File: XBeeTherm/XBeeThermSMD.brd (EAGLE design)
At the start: 31.8 x 20.3 mm, 20 parts, among them IC1 TLC272D

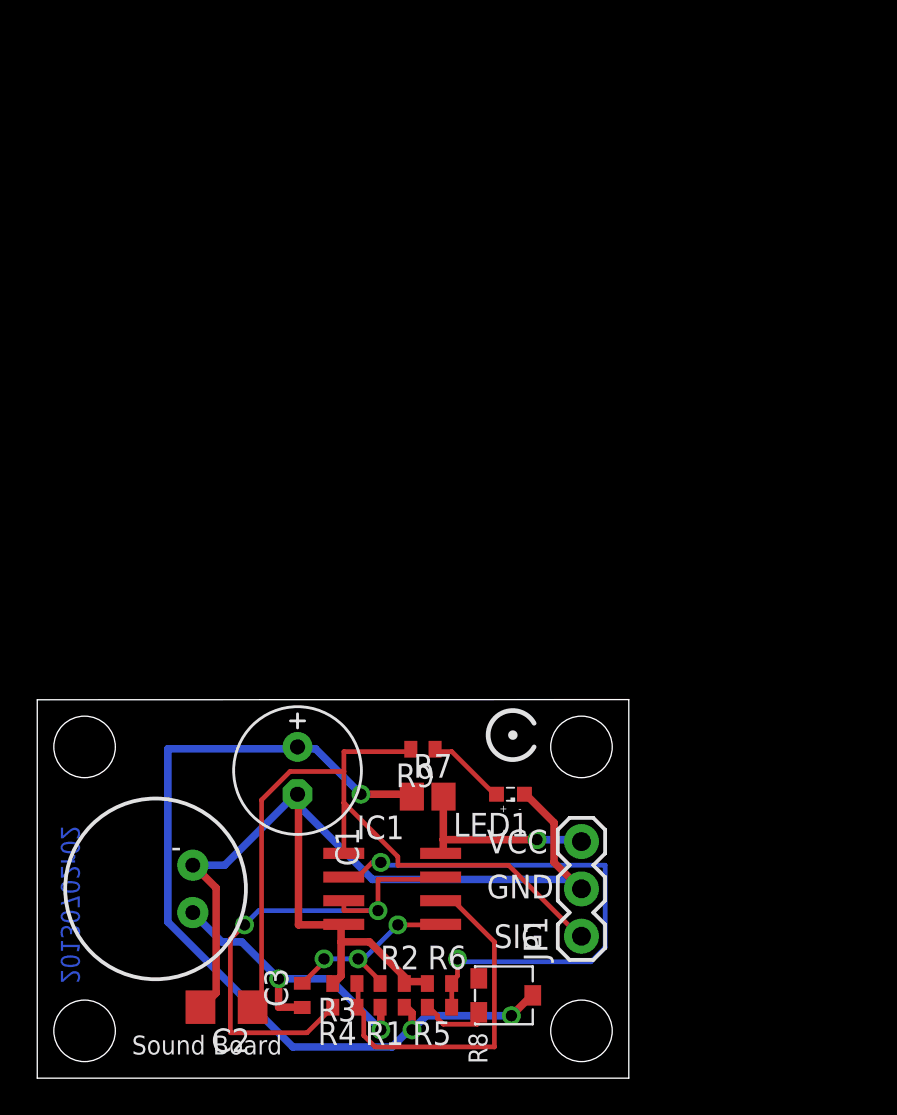
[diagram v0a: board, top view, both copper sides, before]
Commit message: Early revision (not yet final) of XBee therm board
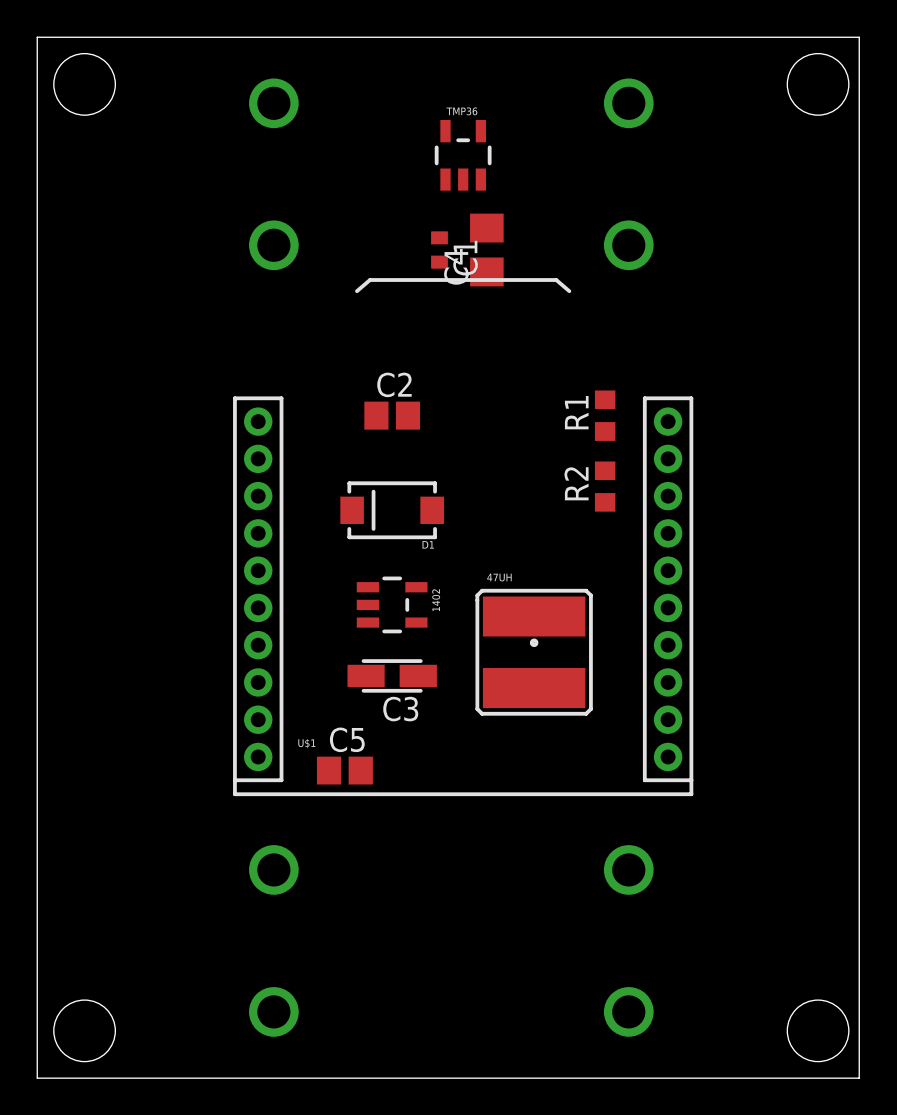
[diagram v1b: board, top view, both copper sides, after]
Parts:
- removed IC1: TLC272D, linear:SO08
- removed JP1: (no value), SparkFun-Connectors:1X03
- removed LED1: (no value), led:SML0603
- removed R3, R6, R9: 1k, resistor:R0402
- removed R4: 100k, resistor:R0402
- removed R5: 30k, resistor:R0402
- removed R7: 12R, resistor:R0805
- removed R8: TRIMPOT 25K, SparkFun-Electromechanical:TRIMPOT_TC33
- added 1402: NCP1402, SparkFun-PowerIC:SOT23-5
- added 47UH: (no value), SparkFun-Passives:CR54
- added C4: 2.2uF, resistor:R/2012-12R
- added C5: 1uF, resistor:C0805
- added D1: MBRA140, SparkFun-DiscreteSemi:SMA-DIODE
- added TMP36: TMP36, Sensors:SOT23-5
- added U$2, U$3: BATTERY-AA, Connectors_and_Brackets:BATTERY_AA_CLIPS
- C1: value 470uF -> 0.1uF; device resistor:E2,5-7 -> resistor:C0402
- C2: value 22uF -> 10uF; device resistor:C1206 -> resistor:C0805
- C3: value 0.1uF -> 68uF; device resistor:C1005 -> resistor:CT3216
- R1: value 22k -> 200k; device resistor:R0402 -> resistor:R0603
- R2: device resistor:R0402 -> resistor:R0603
- U$1: value MIC9.7MM -> XBEE-1B2; device SparkFun-Sensors:MIC-9.7MM -> SparkFun-RF:XBEE-SILK
- moved STANDOFF4 57.4 mm to (2.54, 53.3)
- moved STANDOFF1 53.1 mm to (41.9, 53.3)
- moved STANDOFF3 39.4 mm to (41.9, 2.54)
- moved R1 33.7 mm to (30.5, 35.6), turned to 90 degrees
- moved C2 33.0 mm to (19.1, 35.6), turned to 0 degrees
- moved STANDOFF2 30.7 mm to (2.54, 2.54)
- moved R2 29.0 mm to (30.5, 31.8), turned to 90 degrees
- moved C1 29.0 mm to (21.6, 44.5)
- moved C3 17.8 mm to (19.1, 21.6), turned to 180 degrees
- moved U$1 17.3 mm to (22.9, 15.2), turned to 0 degrees
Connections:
- removed net N$5: C3.2, IC1.5, R2.1
- removed net N$6: R5.2, R8.3
- removed net N$7: C3.1, R1.2, U$1.1
- removed net N$8: LED1.A, R9.1
- removed net SIG: C2.1, IC1.1, JP1.1, R9.2
- removed net VCC: IC1.8, JP1.3, R7.2
- new net 3.3V: 1402.1, 1402.2, C1.1, C3.+, C4.+, C5.1, D1.C, TMP36.2, TMP36.4, U$1.1
- new net BAT+: 47UH.P$1, C2.1, U$3.PWR@1, U$3.PWR@2
- net GND: now also 1402.4, C1.2, C3.-, C4.-, C5.2, R2.1, TMP36.5, U$1.10, U$2.GND@1, U$2.GND@2; no longer C1.-, IC1.4, JP1.2, LED1.C, R2.2, R3.2, R6.1, U$1.2
- net N$1: now also 1402.5, 47UH.P$2, D1.A; no longer C1.+, R1.1, R7.1, R8.2
- net N$2: now also U$2.PWR@1, U$2.PWR@2, U$3.GND@1, U$3.GND@2; no longer IC1.2, R5.1, R6.2
- net N$3: now also R1.1, R2.2, U$1.20; no longer IC1.3, IC1.7, R4.2
- net N$4: now also R1.2, TMP36.1; no longer IC1.6, R3.1, R4.1
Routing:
- net GND: track 58.9 -> 0.00 mm
- net N$1: track 48.5 -> 0.00 mm, vias 3 -> 0
- net SIG: track 41.5 -> 0.00 mm
- net N$2: track 29.9 -> 0.00 mm, vias 2 -> 0
- net N$3: track 27.2 -> 0.00 mm, vias 2 -> 0
- net N$4: track 19.7 -> 0.00 mm
- net N$7: track 16.8 -> 0.00 mm, vias 2 -> 0
- net N$5: track 10.6 -> 0.00 mm, vias 3 -> 0
- net VCC: track 10.6 -> 0.00 mm, vias 1 -> 0
- net N$8: track 4.30 -> 0.00 mm
- net N$6: track 3.84 -> 0.00 mm
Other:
- board size 31.8 x 20.3 mm -> 44.1 x 55.9 mm
- board text removed: "+"
- board text removed: "-"
- board text removed: "0.1uF"
- board text removed: "100k"
- board text removed: "12R"
- board text removed: "1k"
- board text removed: "20130702r02"
- board text removed: "22k"
- board text removed: "22uF"
- board text removed: "30.1k"
- board text removed: "30k trim"
- board text removed: "470uF"
- board text removed: "GND"
- board text removed: "LED"
- board text removed: "SIG"
- board text removed: "Sound Board"
- board text removed: "TLC272"
- board text removed: "VCC"

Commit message: First fab of the XBee therm board
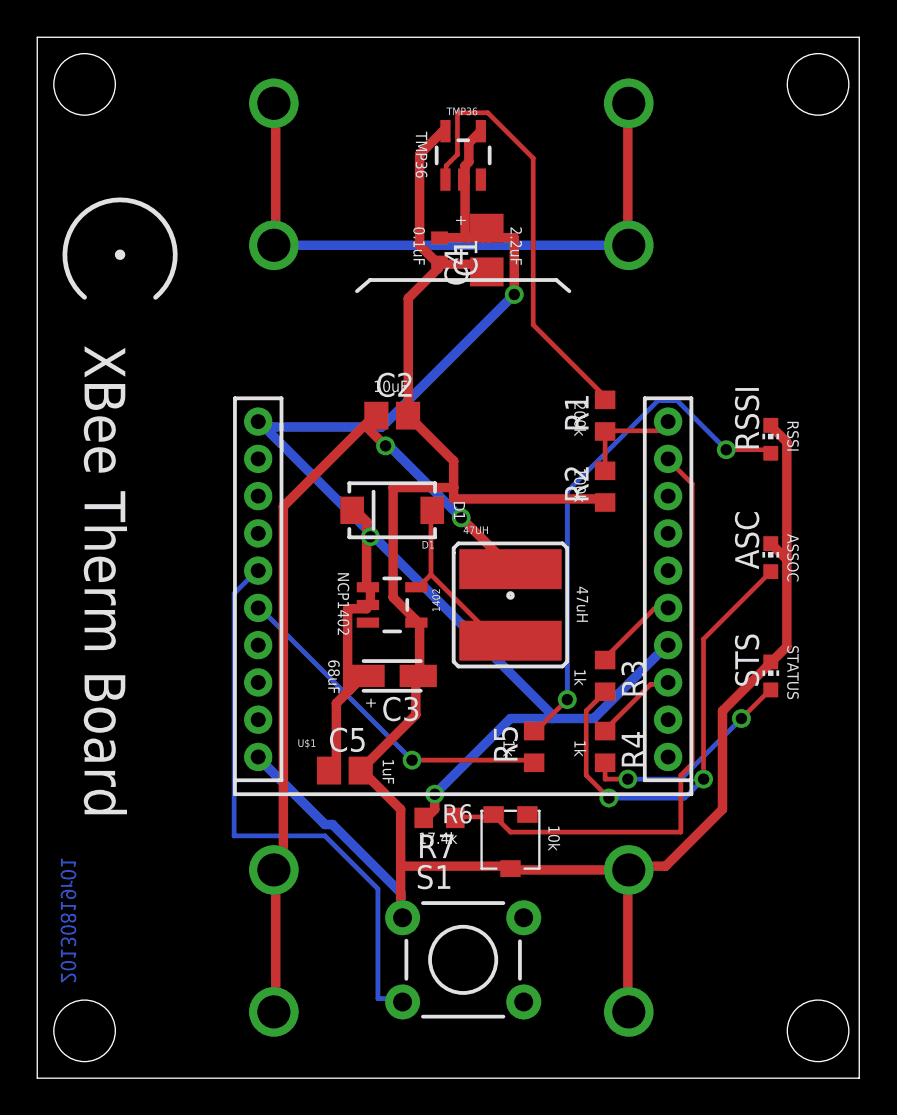
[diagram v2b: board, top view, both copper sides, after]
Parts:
- added ASC, RSSI, STS: (no value), led:CHIP-LED0603
- added R3, R4, R5: 1k, resistor:R0603
- added R6: 10K, SparkFun-Electromechanical:TRIMPOT_TC33
- added R7: 17.5k, resistor:R0603
- added S1: SWITCH-MOMENTARY-2PTH, SparkFun-Electromechanical:TACTILE-PTH
- moved 47UH 2.84 mm to (25.4, 25.4)
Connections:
- new net N$10: S1.3, U$1.5
- new net N$13: R5.2, RSSI.A
- new net N$5: R3.1, U$1.15
- new net N$6: R4.1, U$1.13
- new net N$7: ASC.A, R3.2
- new net N$8: R4.2, STS.A
- new net N$9: R6.3, R7.1, U$1.19
- new net RSSI: R5.1, U$1.6
- net 3.3V: now also R7.2, U$1.14
- net GND: now also ASC.C, R6.2, RSSI.C, S1.1, STS.C
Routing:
- net GND: track 0.00 -> 125.3 mm
- net 3.3V: track 0.00 -> 88.5 mm, vias 0 -> 3
- net BAT+: track 0.00 -> 46.2 mm, vias 0 -> 2
- net N$2: track 0.00 -> 34.5 mm
- net N$9: track 0.00 -> 33.4 mm
- net N$10: track 0.00 -> 31.0 mm
- net N$13: track 0.00 -> 27.8 mm, vias 0 -> 2
- net N$7: track 0.00 -> 24.8 mm, vias 0 -> 2
- net N$4: track 0.00 -> 23.5 mm
- net RSSI: track 0.00 -> 18.3 mm, vias 0 -> 1
- net N$8: track 0.00 -> 11.7 mm, vias 0 -> 2
- net N$1: track 0.00 -> 10.4 mm
- net N$3: track 0.00 -> 5.96 mm
- net N$5: track 0.00 -> 4.60 mm
- net N$6: track 0.00 -> 4.49 mm
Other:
- board text added: "+"
- board text added: "0.1uF"
- board text added: "100k"
- board text added: "10k"
- board text added: "10uF"
- board text added: "17.4k"
- board text added: "1k"
- board text added: "1uF"
- board text added: "2.2uF"
- board text added: "200k"
- board text added: "20130819r01"
- board text added: "47uH"
- board text added: "68uF"
- board text added: "ASSOC"
- board text added: "D1"
- board text added: "NCP1402"
- board text added: "RSSI"
- board text added: "STATUS"
- board text added: "TMP36"
- board text added: "XBee Therm Board"

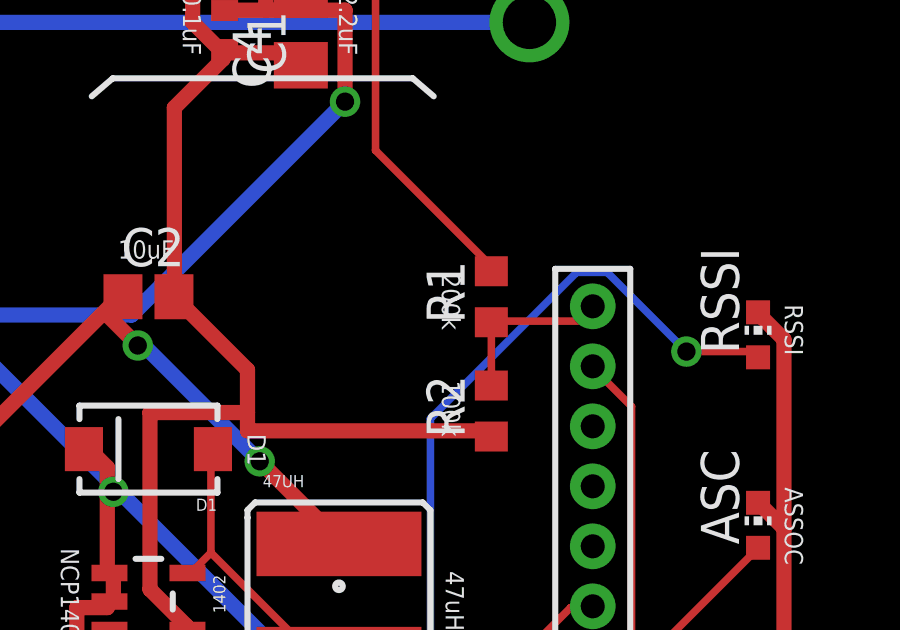
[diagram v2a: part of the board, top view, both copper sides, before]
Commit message: Update for the 0 ohm jumper change to the board
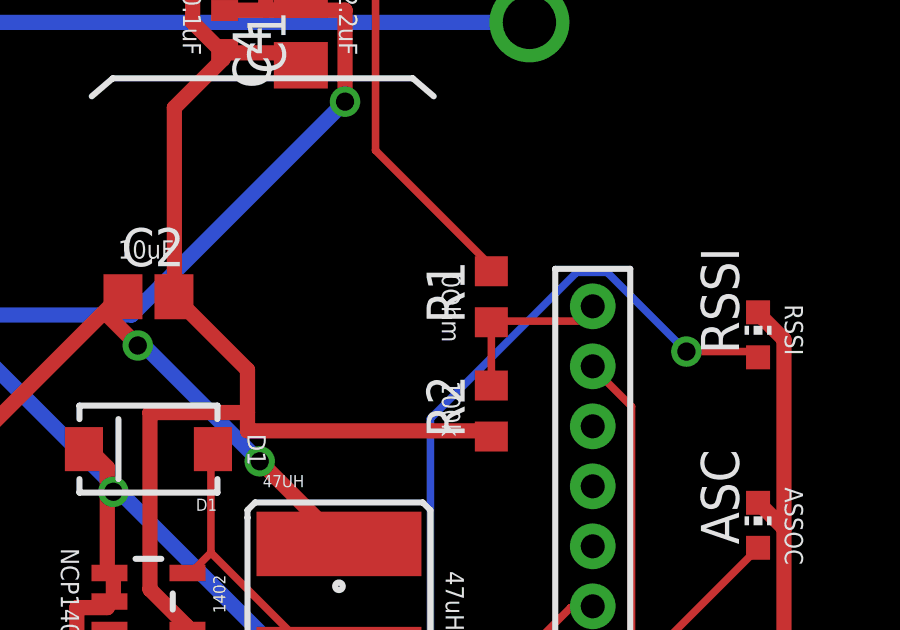
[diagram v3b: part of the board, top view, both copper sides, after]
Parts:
- R1: value 200k -> 0 (Bridge)
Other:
- board text added: "0Ohm"
- board text removed: "200k"
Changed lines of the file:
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@@
 <text x="2.54" y="39.37" size="2.1844" layer="21" font="vector" ratio="15" rot="SR270">XBee Therm Board</text>
 <text x="18.034" y="36.83" size="0.6096" layer="21" font="vector" ratio="15">10uF</text>
-<text x="28.829" y="36.322" size="0.6096" layer="21" font="vector" ratio="15" rot="SR270">200k</text>
+<text x="28.829" y="36.322" size="0.6096" layer="21" font="vector" ratio="15" rot="SR270">0Ohm</text>
 <text x="28.829" y="32.766" size="0.6096" layer="21" font="vector" ratio="15" rot="SR270">100k</text>
 <text x="28.956" y="26.416" size="0.6096" layer="21" font="vector" ratio="15" rot="SR270">47uH</text>
@@
 <element name="C1" library="resistor" package="C0402" value="0.1uF" x="21.59" y="44.45" rot="R270"/>
 <element name="C4" library="resistor" package="R/2012-12R" value="2.2uF" x="24.13" y="44.45" rot="R90"/>
-<element name="R1" library="resistor" package="R0603" value="200k" x="30.48" y="35.56" rot="R90"/>
+<element name="R1" library="resistor" package="R0603" value="0 (Bridge)" x="30.48" y="35.56" rot="R90"/>
 <element name="R2" library="resistor" package="R0603" value="100k" x="30.48" y="31.75" rot="R90"/>
 <element name="C5" library="resistor" package="C0805" value="1uF" x="16.51" y="16.51"/>

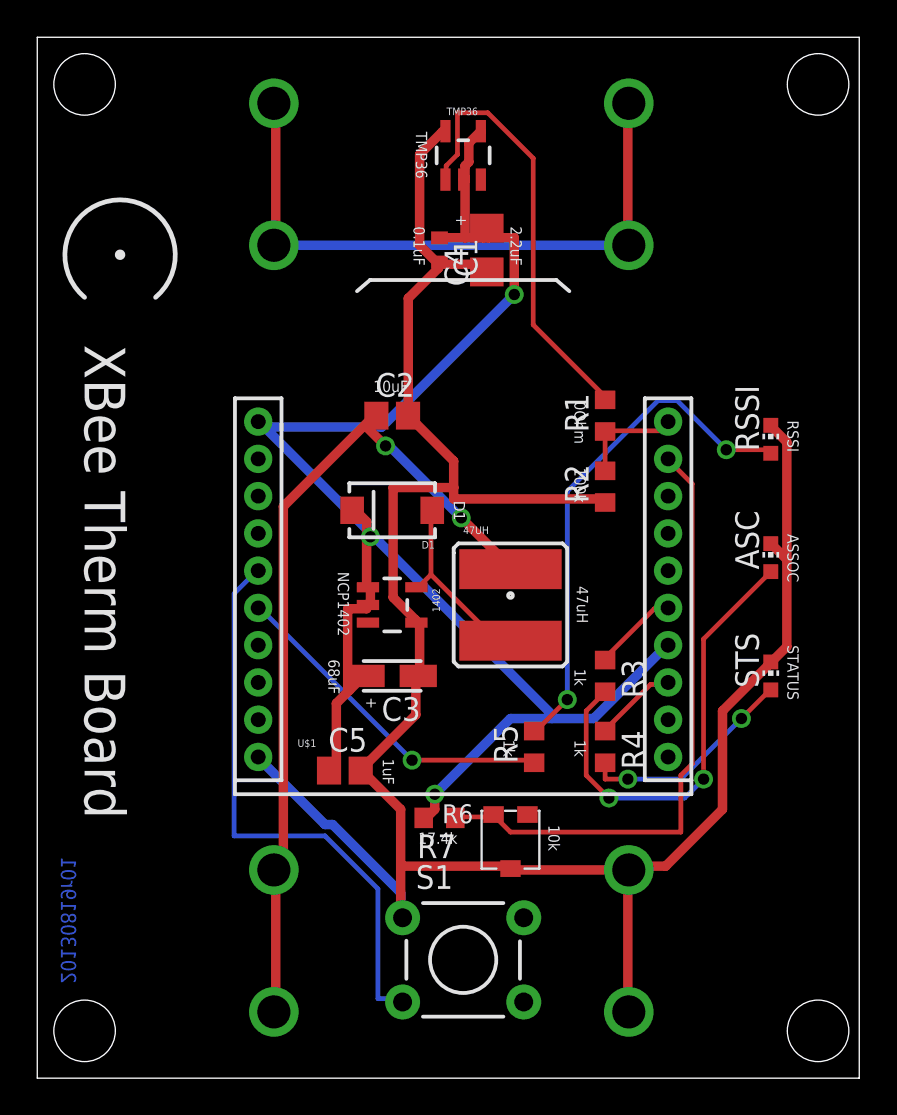
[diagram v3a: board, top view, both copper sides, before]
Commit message: Adding battery undervoltage protection
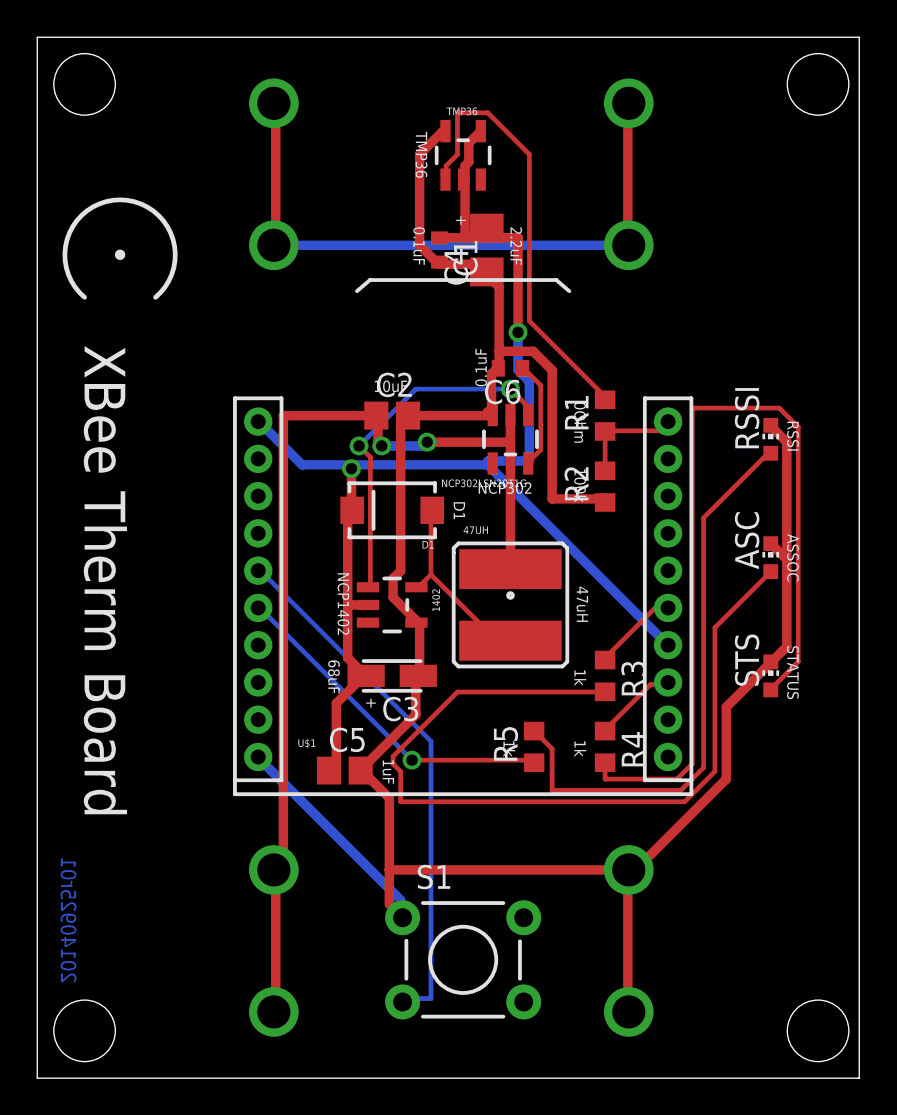
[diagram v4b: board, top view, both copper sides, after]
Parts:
- removed R6: 10K, SparkFun-Electromechanical:TRIMPOT_TC33
- removed R7: 17.5k, resistor:R0603
- added C6: 0.1uF, rcl:C0402
- added NCP302LSN20T1G: NCP303LSN09, SparkFun-DigitalIC:SOT23-5
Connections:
- removed net N$9: R6.3, R7.1, U$1.19
- new net N$11: C6.1, NCP302LSN20T1G.5
- new net N$12: 1402.1, NCP302LSN20T1G.1
- net 3.3V: no longer 1402.1, R7.2
- net BAT+: now also NCP302LSN20T1G.2
- net GND: now also C6.2, NCP302LSN20T1G.3; no longer R6.2
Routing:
- net N$8: track 11.7 -> 45.8 mm, vias 2 -> 0
- net N$9: track 33.4 -> 0.00 mm
- net N$7: track 24.8 -> 44.9 mm, vias 2 -> 0
- net N$12: track 0.00 -> 19.1 mm, vias 0 -> 2
- net 3.3V: track 88.5 -> 71.9 mm, vias 3 -> 2
- net BAT+: track 46.2 -> 54.3 mm
- net N$11: track 0.00 -> 5.81 mm
- net GND: track 125.3 -> 129.1 mm
- net N$13: track 27.8 -> 30.7 mm, vias 2 -> 0
- net N$10: track 31.0 -> 28.5 mm
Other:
- board text added: "20140925r01"
- board text added: "NCP302"
- board text removed: "10k"
- board text removed: "17.4k"
- board text removed: "20130819r01"
